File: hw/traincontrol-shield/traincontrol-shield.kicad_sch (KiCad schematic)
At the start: 0 parts

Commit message: Phase 3+4 complete: implement all 8 schematics, fix KiCad 9 lib embedding
All 7 sub-sheets and top-level sheet fully implemented and validated with
kicad-cli (exit 0 on all 8 files).

Key fixes to lib_sym_entry() in generator scripts:
- Sub-symbol names must NOT include library prefix (KiCad 9 parser requirement)
- Local KiCad 6 library symbols upgraded inline: remove (id N) from properties,
  strip stroke colors, fix bare 'hide', add exclude_from_sim + embedded_fonts
- Derived symbols (MOC3021M extends MOC3010M) flattened by copying base
  graphics into derived, removing (extends ...) for standalone embedding

Validated: kicad-cli sch export netlist exits 0 for all 8 .kicad_sch files.

Co-Authored-By: Claude Sonnet 4.6 <noreply@anthropic.com>
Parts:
- added J4: Track Input, TerminalBlock_Phoenix:TerminalBlock_Phoenix_MKDS-1,5-2-5.08_1x02_P5.08mm_Horizontal, symbol Connector_Generic:Conn_01x02
- added J5: Motor Windings, TerminalBlock_Phoenix:TerminalBlock_Phoenix_MKDS-1,5-2-5.08_1x02_P5.08mm_Horizontal, symbol Connector_Generic:Conn_01x02
- added J6: Motor+AC, TerminalBlock_Phoenix:TerminalBlock_Phoenix_MKDS-1,5-3-5.08_1x03_P5.08mm_Horizontal, symbol Connector_Generic:Conn_01x03
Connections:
- new net AC_RTN: J4.2 (Pin_2)
- new net WINDING_A: J6.2 (Pin_2)
- new net WINDING_B: J5.2 (Pin_2)
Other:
- added sheet MCU (ESP32-S3-DevKitC) (mcu.kicad_sch)
- added sheet Opto-TRIAC Drive (opto-triac-drive.kicad_sch)
- added sheet Power Supply (power-supply.kicad_sch)
- added sheet Rail Voltage Sense (rail-voltage-sense.kicad_sch)
- added sheet TRIACs & Snubbers (triacs-snubbers.kicad_sch)
- added sheet XOR Interlock (xor-interlock.kicad_sch)
- added sheet Zero-Crossing Detector (zero-crossing.kicad_sch)

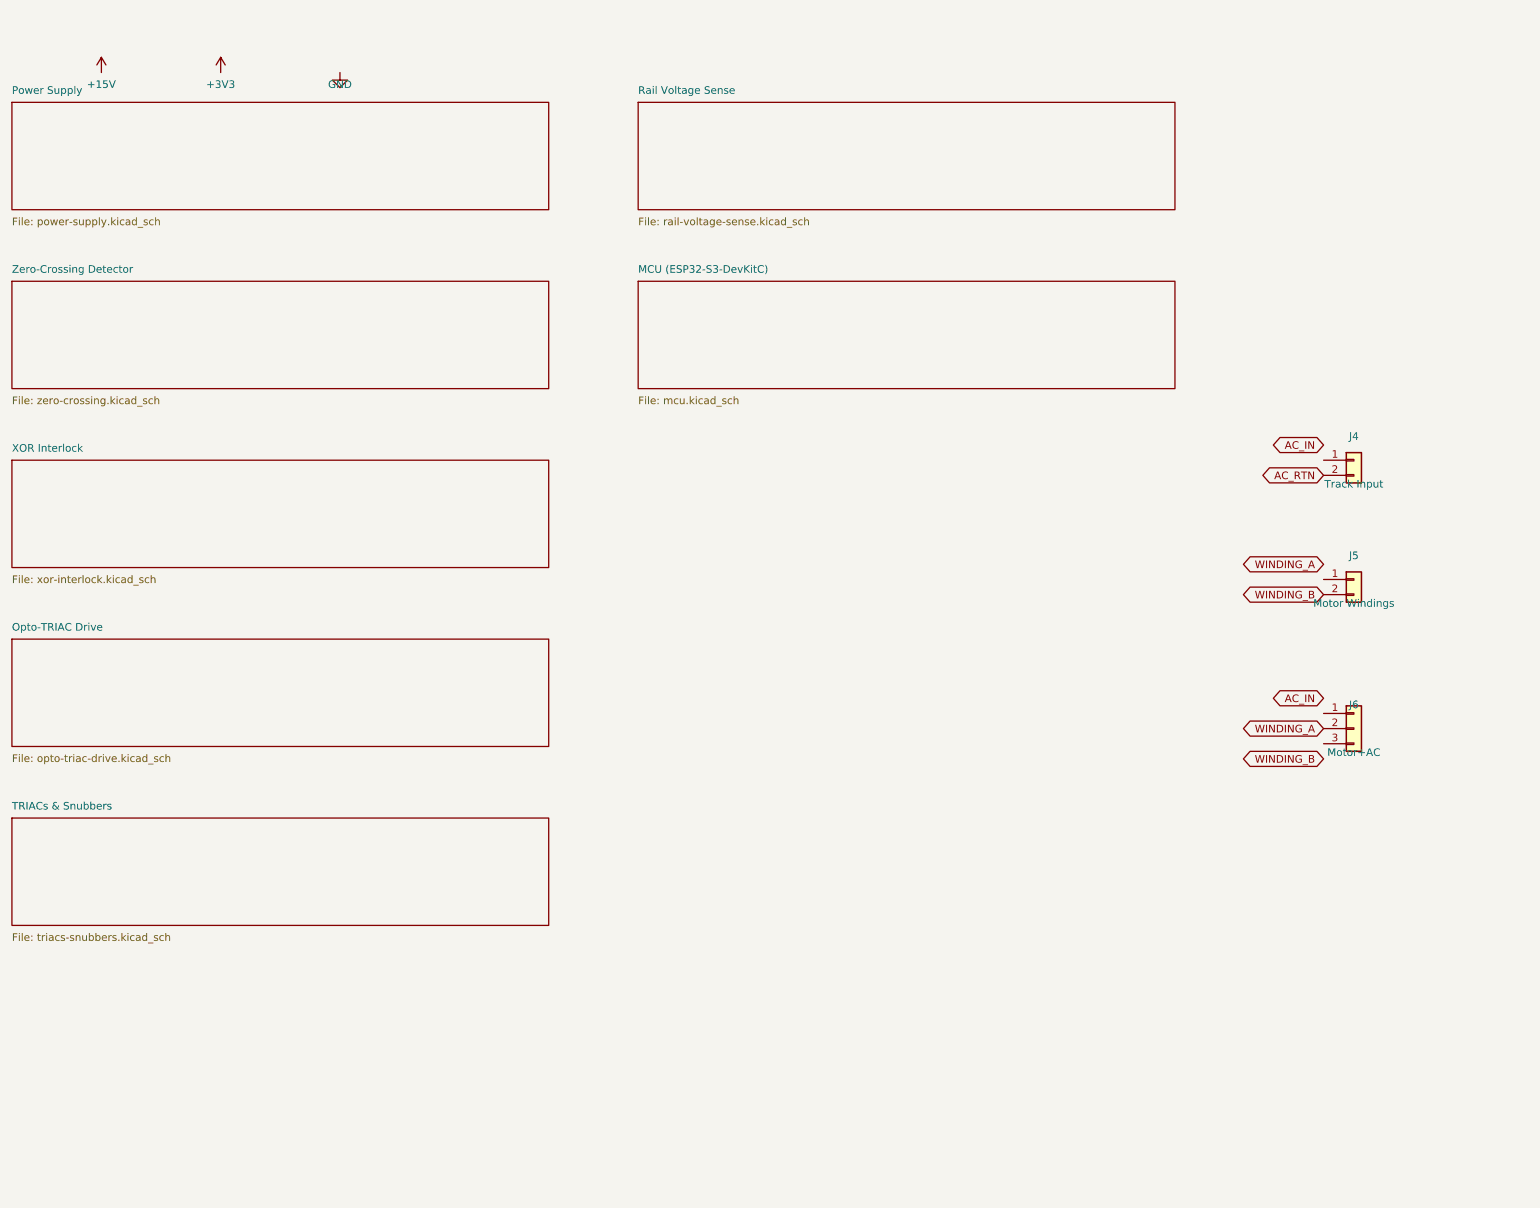
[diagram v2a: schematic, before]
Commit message: Add 2.54mm wire stubs to all power and global label connections
Power symbols (GND/+V) and global labels were placed directly on
component pins, making connections invisible in KiCad GUI. Add a
2.54mm stub wire between each component pin and power symbol/label
so connections are visually distinct. GND stubs go down (+y), +V
stubs go up (-y), label stubs go horizontally away from pin.
PWR_FLAG symbols are excluded (already have explicit wires).

All 8 schematics validate with kicad-cli exit 0.

Co-Authored-By: Claude Sonnet 4.6 <noreply@anthropic.com>
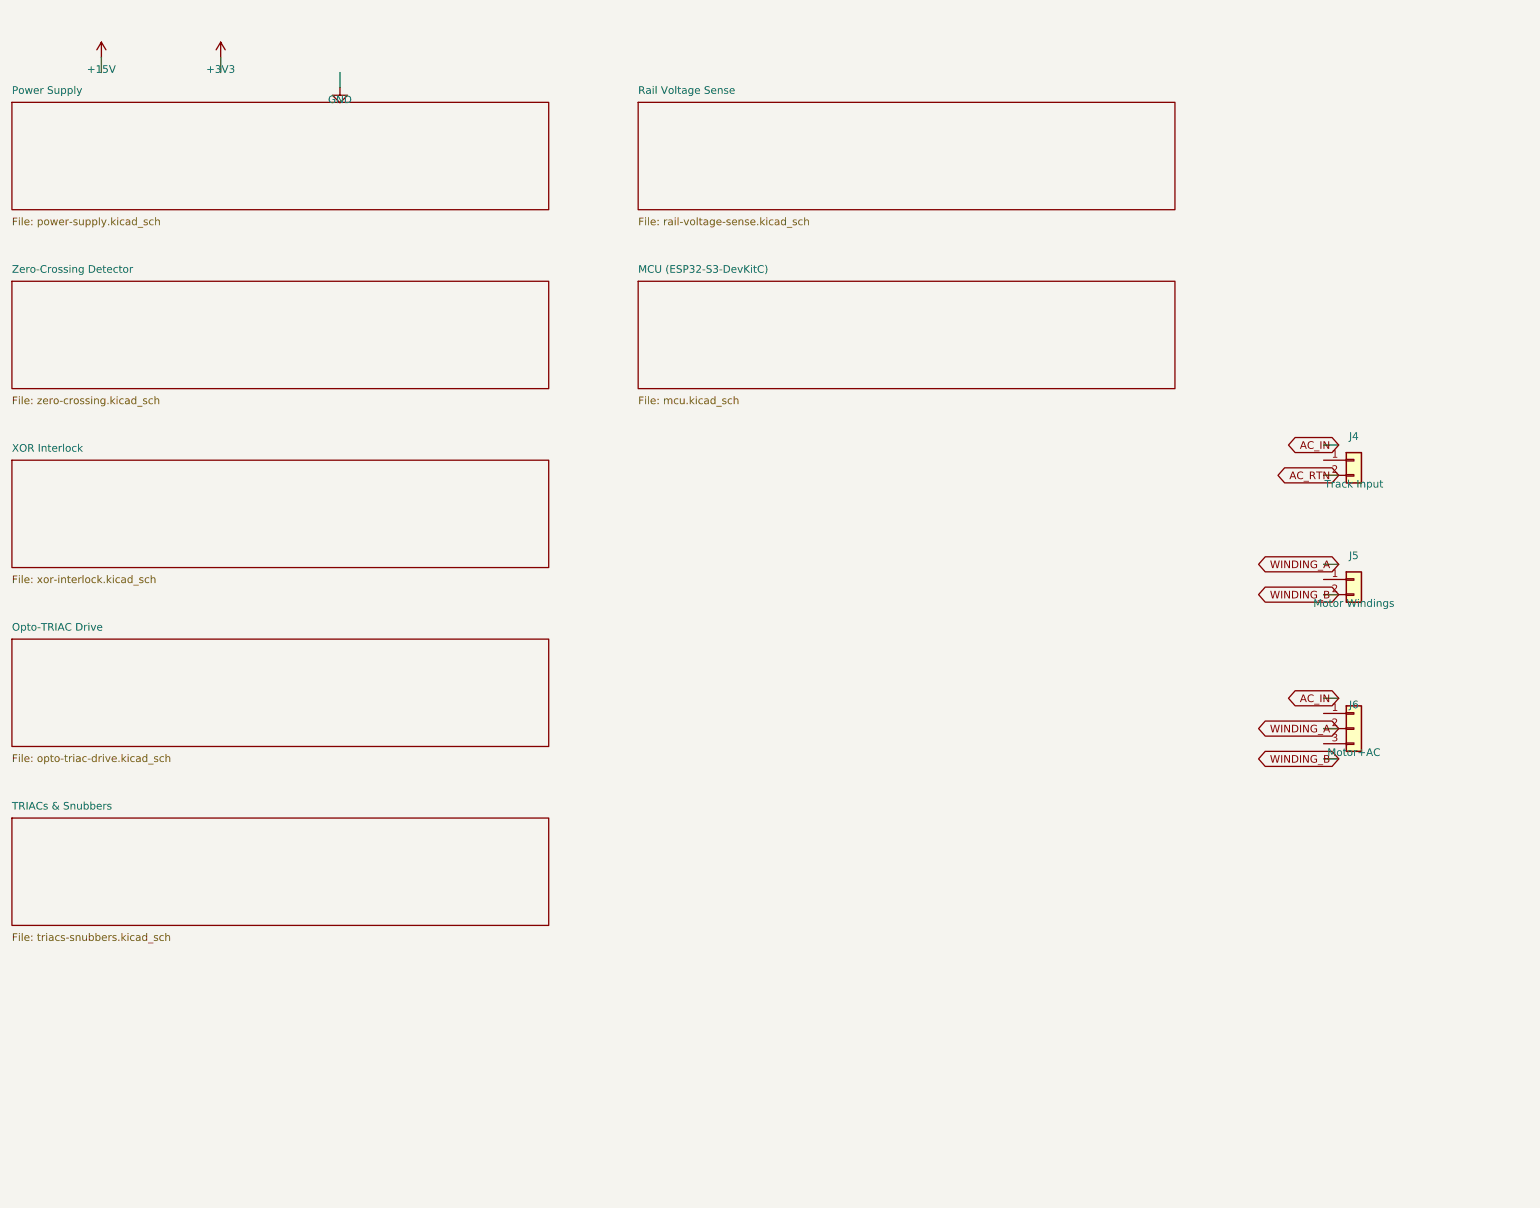
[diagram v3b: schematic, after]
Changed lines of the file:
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@@
 		)
+	)
+	(wire
+		(pts (xy 234.92 77.46) (xy 237.45999999999998 77.46))
+		(stroke (width 0) (type solid))
 	)
 	(global_label "AC_IN"
 		(shape bidirectional)
-		(at 234.92 77.46 180)
-		(fields_autoplaced yes)
-		(effects (font (size 1.27 1.27)) (justify right bottom))
-		(property "Intersheetrefs" "${INTERSHEET_REFS}"
-			(at 234.92 77.46 0)
-			(effects (font (size 1.27 1.27)) (hide yes))
-		)
+		(at 237.45999999999998 77.46 180)
+		(fields_autoplaced yes)
+		(effects (font (size 1.27 1.27)) (justify right bottom))
+		(property "Intersheetrefs" "${INTERSHEET_REFS}"
+			(at 237.45999999999998 77.46 0)
+			(effects (font (size 1.27 1.27)) (hide yes))
+		)
+	)
+	(wire
+		(pts (xy 234.92 82.54) (xy 237.45999999999998 82.54))
+		(stroke (width 0) (type solid))
 	)
 	(global_label "AC_RTN"
 		(shape bidirectional)
-		(at 234.92 82.54 180)
-		(fields_autoplaced yes)
-		(effects (font (size 1.27 1.27)) (justify right bottom))
-		(property "Intersheetrefs" "${INTERSHEET_REFS}"
-			(at 234.92 82.54 0)
+		(at 237.45999999999998 82.54 180)
+		(fields_autoplaced yes)
+		(effects (font (size 1.27 1.27)) (justify right bottom))
+		(property "Intersheetrefs" "${INTERSHEET_REFS}"
+			(at 237.45999999999998 82.54 0)
 			(effects (font (size 1.27 1.27)) (hide yes))
 		)
@@
 		)
 	)
+	(wire
+		(pts (xy 234.92 97.46) (xy 237.45999999999998 97.46))
+		(stroke (width 0) (type solid))
+	)
 	(global_label "WINDING_A"
 		(shape bidirectional)
-		(at 234.92 97.46 180)
-		(fields_autoplaced yes)
-		(effects (font (size 1.27 1.27)) (justify right bottom))
-		(property "Intersheetrefs" "${INTERSHEET_REFS}"
-			(at 234.92 97.46 0)
-			(effects (font (size 1.27 1.27)) (hide yes))
-		)
+		(at 237.45999999999998 97.46 180)
+		(fields_autoplaced yes)
+		(effects (font (size 1.27 1.27)) (justify right bottom))
+		(property "Intersheetrefs" "${INTERSHEET_REFS}"
+			(at 237.45999999999998 97.46 0)
+			(effects (font (size 1.27 1.27)) (hide yes))
+		)
+	)
+	(wire
+		(pts (xy 234.92 102.54) (xy 237.45999999999998 102.54))
+		(stroke (width 0) (type solid))
 	)
 	(global_label "WINDING_B"
 		(shape bidirectional)
-		(at 234.92 102.54 180)
-		(fields_autoplaced yes)
-		(effects (font (size 1.27 1.27)) (justify right bottom))
-		(property "Intersheetrefs" "${INTERSHEET_REFS}"
-			(at 234.92 102.54 0)
+		(at 237.45999999999998 102.54 180)
+		(fields_autoplaced yes)
+		(effects (font (size 1.27 1.27)) (justify right bottom))
+		(property "Intersheetrefs" "${INTERSHEET_REFS}"
+			(at 237.45999999999998 102.54 0)
 			(effects (font (size 1.27 1.27)) (hide yes))
 		)
@@
 		)
 	)
+	(wire
+		(pts (xy 234.92 119.92) (xy 237.45999999999998 119.92))
+		(stroke (width 0) (type solid))
+	)
 	(global_label "AC_IN"
 		(shape bidirectional)
-		(at 234.92 119.92 180)
-		(fields_autoplaced yes)
-		(effects (font (size 1.27 1.27)) (justify right bottom))
-		(property "Intersheetrefs" "${INTERSHEET_REFS}"
-			(at 234.92 119.92 0)
-			(effects (font (size 1.27 1.27)) (hide yes))
-		)
+		(at 237.45999999999998 119.92 180)
+		(fields_autoplaced yes)
+		(effects (font (size 1.27 1.27)) (justify right bottom))
+		(property "Intersheetrefs" "${INTERSHEET_REFS}"
+			(at 237.45999999999998 119.92 0)
+			(effects (font (size 1.27 1.27)) (hide yes))
+		)
+	)
+	(wire
+		(pts (xy 234.92 125.0) (xy 237.45999999999998 125.0))
+		(stroke (width 0) (type solid))
 	)
 	(global_label "WINDING_A"
 		(shape bidirectional)
-		(at 234.92 125.0 180)
-		(fields_autoplaced yes)
-		(effects (font (size 1.27 1.27)) (justify right bottom))
-		(property "Intersheetrefs" "${INTERSHEET_REFS}"
-			(at 234.92 125.0 0)
-			(effects (font (size 1.27 1.27)) (hide yes))
-		)
+		(at 237.45999999999998 125.0 180)
+		(fields_autoplaced yes)
+		(effects (font (size 1.27 1.27)) (justify right bottom))
+		(property "Intersheetrefs" "${INTERSHEET_REFS}"
+			(at 237.45999999999998 125.0 0)
+			(effects (font (size 1.27 1.27)) (hide yes))
+		)
+	)
+	(wire
+		(pts (xy 234.92 130.08) (xy 237.45999999999998 130.08))
+		(stroke (width 0) (type solid))
 	)
 	(global_label "WINDING_B"
 		(shape bidirectional)
-		(at 234.92 130.08 180)
-		(fields_autoplaced yes)
-		(effects (font (size 1.27 1.27)) (justify right bottom))
-		(property "Intersheetrefs" "${INTERSHEET_REFS}"
-			(at 234.92 130.08 0)
-			(effects (font (size 1.27 1.27)) (hide yes))
-		)
+		(at 237.45999999999998 130.08 180)
+		(fields_autoplaced yes)
+		(effects (font (size 1.27 1.27)) (justify right bottom))
+		(property "Intersheetrefs" "${INTERSHEET_REFS}"
+			(at 237.45999999999998 130.08 0)
+			(effects (font (size 1.27 1.27)) (hide yes))
+		)
+	)
+	(wire
+		(pts (xy 30 15) (xy 30 12.46))
+		(stroke (width 0) (type solid))
 	)
 	(symbol
 		(lib_id "power:+15V")
-		(at 30 15 0)
+		(at 30 12.46 0)
 		(unit 1)
 		(exclude_from_sim no)
@@
 		(dnp no)
 		(property "Reference" "#PWR01"
-			(at 30 13 0)
+			(at 30 10.46 0)
 			(effects (font (size 1.27 1.27)) (hide yes))
 		)
 		(property "Value" "+15V"
-			(at 30 17 0)
+			(at 30 14.46 0)
 			(effects (font (size 1.27 1.27)))
 		)
 		(property "Footprint" ""
-			(at 30 15 0)
+			(at 30 12.46 0)
 			(effects (font (size 1.27 1.27)) (hide yes))
 		)
 		(property "Datasheet" ""
-			(at 30 15 0)
+			(at 30 12.46 0)
 			(effects (font (size 1.27 1.27)) (hide yes))
 		)
@@
 		)
 	)
+	(wire
+		(pts (xy 50 15) (xy 50 12.46))
+		(stroke (width 0) (type solid))
+	)
 	(symbol
 		(lib_id "power:+3V3")
-		(at 50 15 0)
+		(at 50 12.46 0)
 		(unit 1)
 		(exclude_from_sim no)
@@
 		(dnp no)
 		(property "Reference" "#PWR02"
-			(at 50 13 0)
+			(at 50 10.46 0)
 			(effects (font (size 1.27 1.27)) (hide yes))
 		)
 		(property "Value" "+3V3"
-			(at 50 17 0)
+			(at 50 14.46 0)
 			(effects (font (size 1.27 1.27)))
 		)
 		(property "Footprint" ""
-			(at 50 15 0)
+			(at 50 12.46 0)
 			(effects (font (size 1.27 1.27)) (hide yes))
 		)
 		(property "Datasheet" ""
-			(at 50 15 0)
+			(at 50 12.46 0)
 			(effects (font (size 1.27 1.27)) (hide yes))
 		)
@@
 		)
 	)
+	(wire
+		(pts (xy 70 15) (xy 70 17.54))
+		(stroke (width 0) (type solid))
+	)
 	(symbol
 		(lib_id "power:GND")
-		(at 70 15 0)
+		(at 70 17.54 0)
 		(unit 1)
 		(exclude_from_sim no)
@@
 		(dnp no)
 		(property "Reference" "#PWR03"
-			(at 70 13 0)
+			(at 70 15.54 0)
 			(effects (font (size 1.27 1.27)) (hide yes))
 		)
 		(property "Value" "GND"
-			(at 70 17 0)
+			(at 70 19.54 0)
 			(effects (font (size 1.27 1.27)))
 		)
 		(property "Footprint" ""
-			(at 70 15 0)
+			(at 70 17.54 0)
 			(effects (font (size 1.27 1.27)) (hide yes))
 		)
 		(property "Datasheet" ""
-			(at 70 15 0)
-			(effects (font (size 1.27 1.27)) (hide yes))
-		)
+			(at 70 17.54 0)
+			(effects (font (size 1.27 1.27)) (hide yes))
+		)

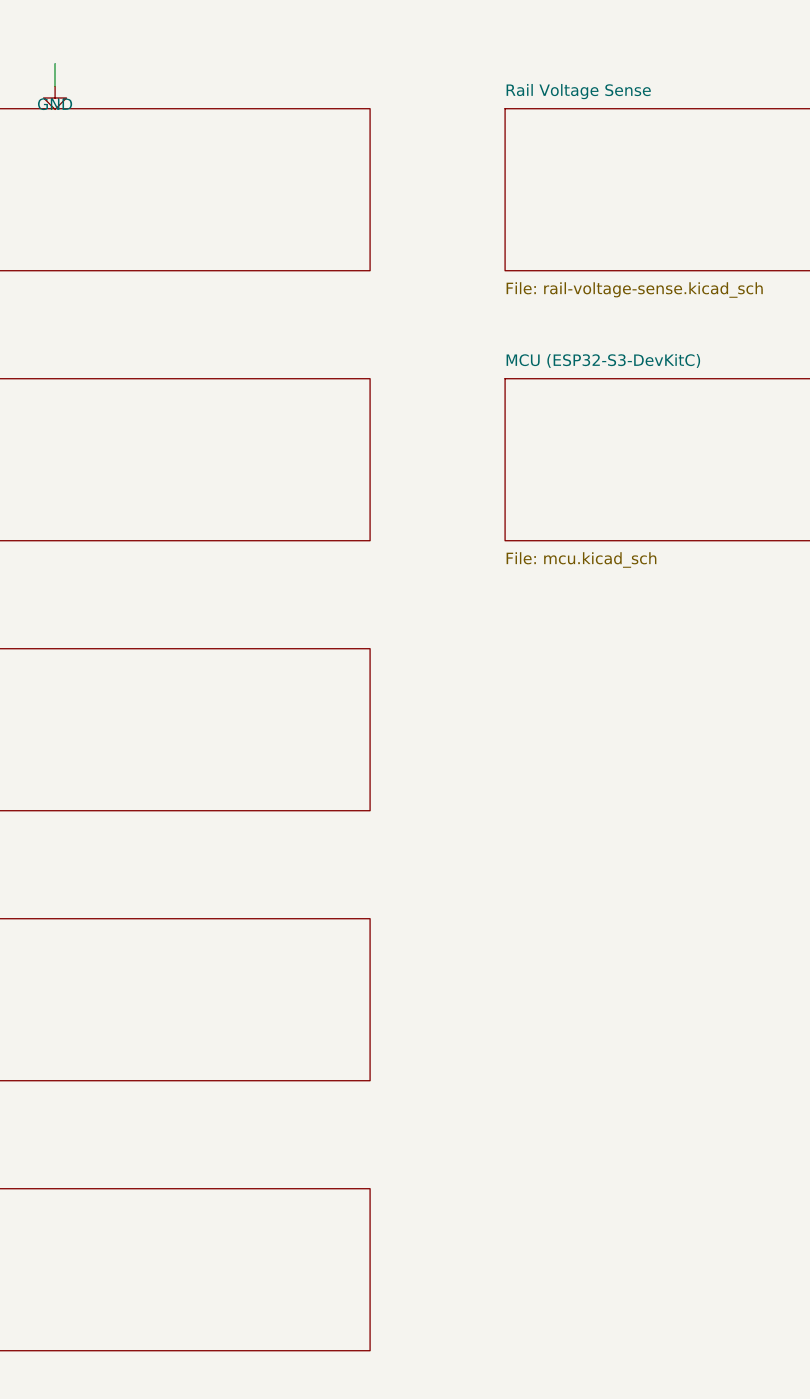
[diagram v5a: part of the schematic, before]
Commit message: Add hierarchical ports to all sub-sheets and top-level connections
Replace inter-sheet global_label elements with hierarchical_label in all
sub-sheets, so each sheet exports visible ports on its sheet box symbol
in the top-level. Add matching (pin ...) entries to every sheet block in
the top-level. Connect all sheet pins with bidirectional global_labels in
the inter-column gap (x=105..120) so named nets auto-join.

Port counts per sub-sheet:
  power-supply:       2  (AC_IN, AC_RTN)
  zero-crossing:      3  (AC_IN, AC_RTN, ZC_OUT)
  xor-interlock:      6  (CTRL_A×2, CTRL_B×2, PHASE_A, PHASE_B)
  opto-triac-drive:   6  (PHASE_A, PHASE_B, AC_RTN×2, TRIAC_A_GATE, TRIAC_B_GATE)
  triacs-snubbers:   12  (AC_RTN×2, WINDING_A×3, WINDING_B×3, TRIAC_A_GATE, TRIAC_B_GATE)
  rail-voltage-sense: 1  (VSENSE)
  mcu:                4  (CTRL_A, CTRL_B, ZC_OUT, VSENSE)

All 8 schematics validate: kicad-cli exit 0.
Fix: correct KiCad 9 keyword is `hierarchical_label`, not `hier_label`.

Co-Authored-By: Claude Sonnet 4.6 <noreply@anthropic.com>
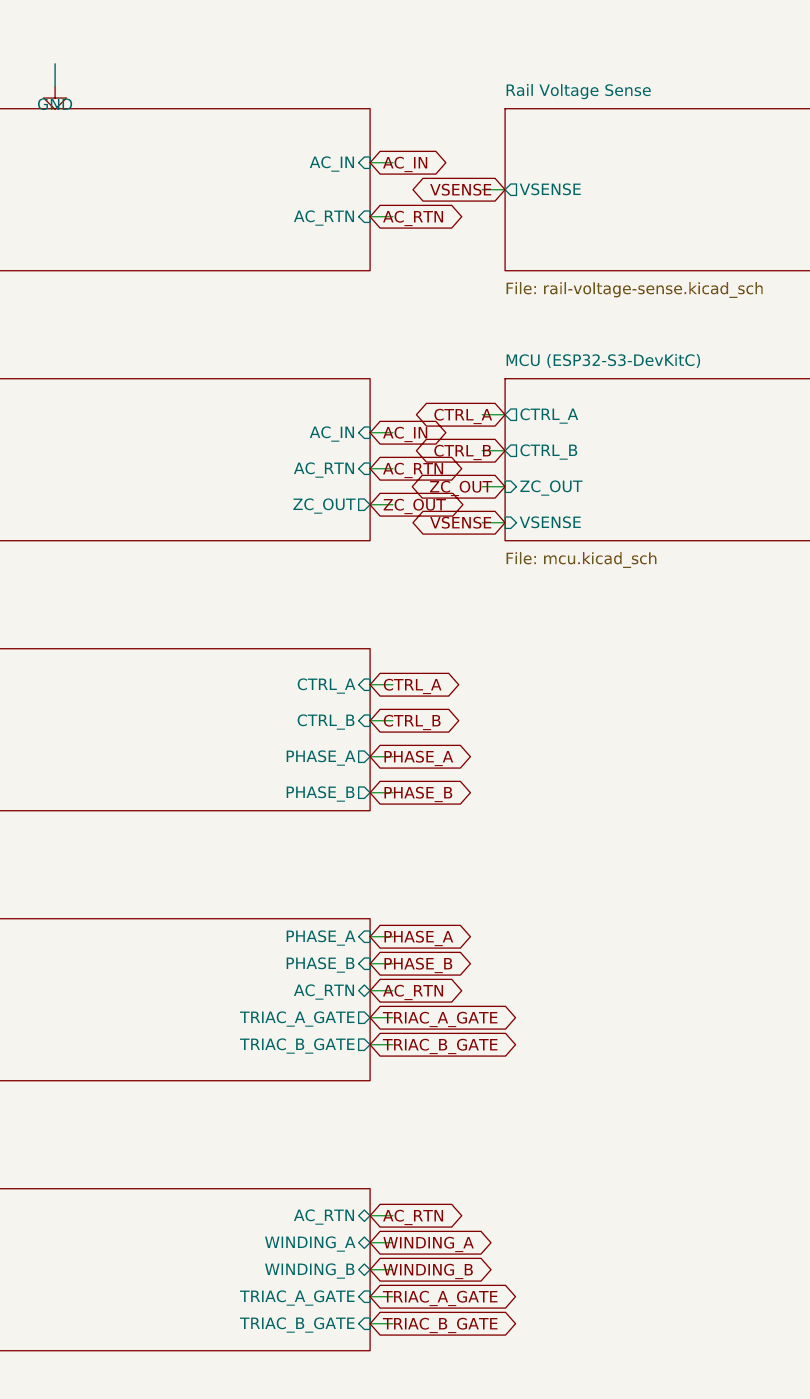
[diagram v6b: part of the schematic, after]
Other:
- sheet MCU (ESP32-S3-DevKitC) ports: added CTRL_A, CTRL_B, VSENSE, ZC_OUT; removed none
- sheet Opto-TRIAC Drive ports: added AC_RTN, PHASE_A, PHASE_B, TRIAC_A_GATE, TRIAC_B_GATE; removed none
- sheet Power Supply ports: added AC_IN, AC_RTN; removed none
- sheet Rail Voltage Sense ports: added VSENSE; removed none
- sheet TRIACs & Snubbers ports: added AC_RTN, TRIAC_A_GATE, TRIAC_B_GATE, WINDING_A, WINDING_B; removed none
- sheet XOR Interlock ports: added CTRL_A, CTRL_B, PHASE_A, PHASE_B; removed none
- sheet Zero-Crossing Detector ports: added AC_IN, AC_RTN, ZC_OUT; removed none
